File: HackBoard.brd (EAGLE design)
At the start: 68.6 x 61.6 mm, 45 parts, among them J1 USB MICRO, J2 8x1F-H8.5, J3 8x1F-H8.5, J4 6x1F-H8.5, P13 Yellow, U1 ATMEGA32U4-XUMU, U2 ATMEGA32U4-XUAU, U3 LP2985-33DBVR, Y1 16MHz KX-7

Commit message: Adición de 2 switch y 3 leds
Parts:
- added A: Amarillo, led:CHIPLED_0805
- added C10, C12: 100n, rcl:C0805
- added R: Rojo, led:CHIPLED_0805
- added R12, R13, R14, R15: 1K, resistor:M0805
- added SW1, SW2: (no value), switch-omron:B3F-10XX
- added V: Verde, led:CHIPLED_0805
- moved C11 0.51 mm to (30.2, 20.2)
- moved C4 0.51 mm to (48.8, 35.4)
- moved C5 0.51 mm to (57.1, 30.4)
- moved C7 0.51 mm to (57.1, 20.2)
- moved C8 0.51 mm to (6.99, 46.2)
- moved C9 0.51 mm to (58.4, 21.8)
- moved D2 0.51 mm to (58.9, 30.4)
- moved ICSP 0.51 mm to (64.9, 31.6)
- moved J1 0.51 mm to (1.45, 41.8)
- moved JP2 0.51 mm to (41.9, 59.2)
- moved L1 0.51 mm to (55.2, 30.4)
- moved L2 0.51 mm to (11.4, 36.7)
- moved ON 0.51 mm to (20.2, 40.8)
- moved R10 0.51 mm to (11.4, 43.3)
- moved R2 0.51 mm to (55.9, 18.0)
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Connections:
- new net LED_A: R14.2
- new net LED_R: R13.2
- new net LED_V: R15.2
- new net N$10: R15.1, V.A
- new net N$8: R.A, R13.1
- new net N$9: A.A, R14.1
- new net SW1: C10.2, SW1.1, SW1.2
- new net SW2: C12.2, R12.2, SW2.3, SW2.4
- net +5V: now also SW2.1, SW2.2
- net GND: now also A.C, C10.1, C12.1, R.C, R12.1, SW1.3, SW1.4, V.C
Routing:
- net +5V: track 258.3 -> 272.9 mm
- net SW2: track 0.00 -> 12.3 mm
- net SW1: track 0.00 -> 11.1 mm
- net N$9: track 0.00 -> 9.92 mm
- net N$8: track 0.00 -> 8.66 mm
- net N$10: track 0.00 -> 8.08 mm
- net GND: track 62.4 -> 63.5 mm, vias 18 -> 17
- net A4: track 24.3 -> 24.8 mm
- net VIN: track 3.56 -> 4.06 mm
- net N$6: track 3.56 -> 4.06 mm
- net A5: track 25.9 -> 26.4 mm
- net A3: track 22.7 -> 23.2 mm
- net A1: track 20.0 -> 20.5 mm
- net A0: track 18.7 -> 19.2 mm
- net A2: track 21.4 -> 21.9 mm
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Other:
- board size 68.6 x 61.6 mm -> 68.6 x 62.1 mm
- board text added: "HackBoard v0.2 hackbo.co"
- board text added: "Made In Colombia"

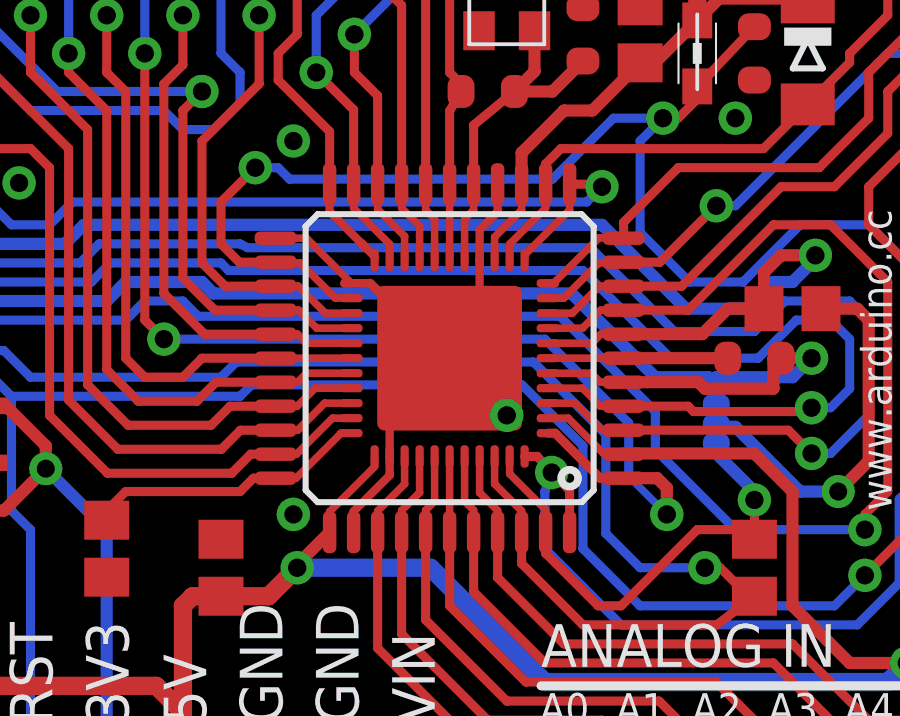
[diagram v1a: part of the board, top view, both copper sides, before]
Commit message: Se elimina Micro con encapsulado QFN
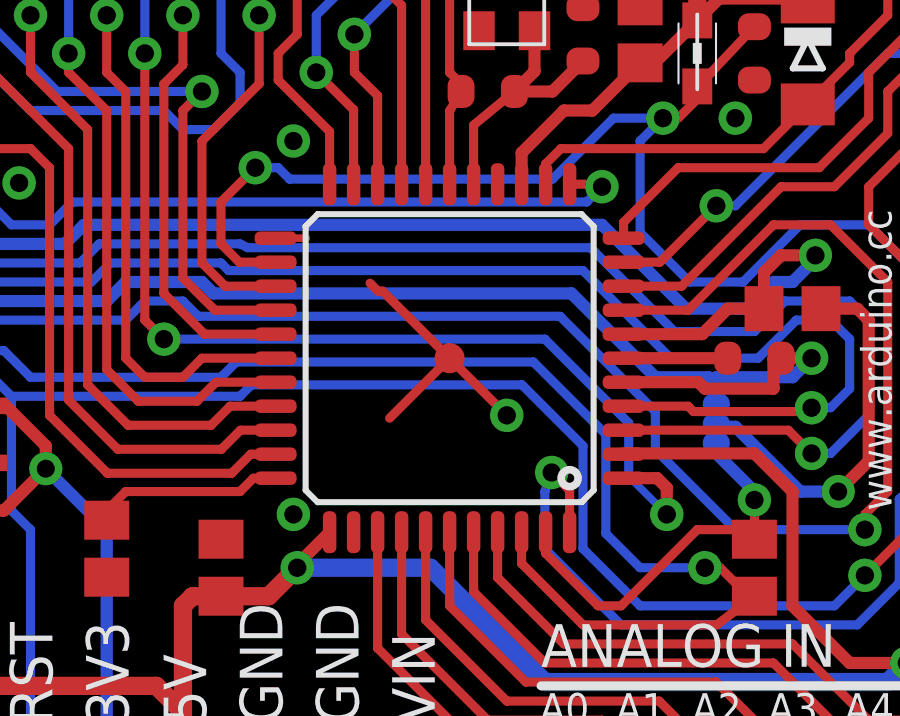
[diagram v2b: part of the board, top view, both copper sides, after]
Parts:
- removed U1: ATMEGA32U4-XUMU, SmartPrj:QFN44ML7X7
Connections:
- net +5V: no longer U1.14, U1.2, U1.34, U1.7
- net A0: no longer U1.36
- net A1: no longer U1.37
- net A2: no longer U1.38
- net A3: no longer U1.39
- net A4: no longer U1.40
- net A5: no longer U1.41
- net AGND: no longer U1.43
- net AREF: no longer U1.42
- net AVCC: no longer U1.24, U1.44
- net D0/RX: no longer U1.20
- net D1/TX: no longer U1.21
- net D2/SDA: no longer U1.19
- net D3/SCL: no longer U1.18
- net D4: no longer U1.25
- net D5*: no longer U1.31
- net D6*: no longer U1.27
- net D7: no longer U1.1
- net GND: no longer U1.15, U1.23, U1.35, U1.EXP
- net HWB: no longer U1.33
- net IO10*: no longer U1.30
- net IO11*: no longer U1.12
- net IO12: no longer U1.26
- net IO13*: no longer U1.32
- net IO8: no longer U1.28
- net IO9*: no longer U1.29
- net MISO: no longer U1.11
- net MOSI: no longer U1.10
- net RD+: no longer U1.4
- net RD-: no longer U1.3
- net RESET: no longer U1.13
- net RXLED: no longer U1.8
- net SCK: no longer U1.9
- net TXLED: no longer U1.22
- net UCAP: no longer U1.6
- net UGND: no longer U1.5
- net XTAL1: no longer U1.17
- net XTAL2: no longer U1.16
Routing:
- net GND: track 63.5 -> 50.0 mm
- net +5V: track 272.9 -> 261.2 mm
- net AVCC: track 73.5 -> 69.4 mm
- net TXLED: track 49.6 -> 46.3 mm
- net MISO: track 20.4 -> 17.2 mm
- net HWB: track 9.54 -> 6.40 mm
- net IO11*: track 62.6 -> 59.5 mm
- net D7: track 68.3 -> 65.1 mm
- net IO13*: track 64.7 -> 61.7 mm
- net D1/TX: track 46.2 -> 43.2 mm
- net AGND: track 16.8 -> 13.7 mm
- net RESET: track 165.9 -> 162.8 mm
- net MOSI: track 19.8 -> 16.8 mm
- net RD-: track 75.6 -> 72.7 mm
- net D5*: track 70.1 -> 67.2 mm
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
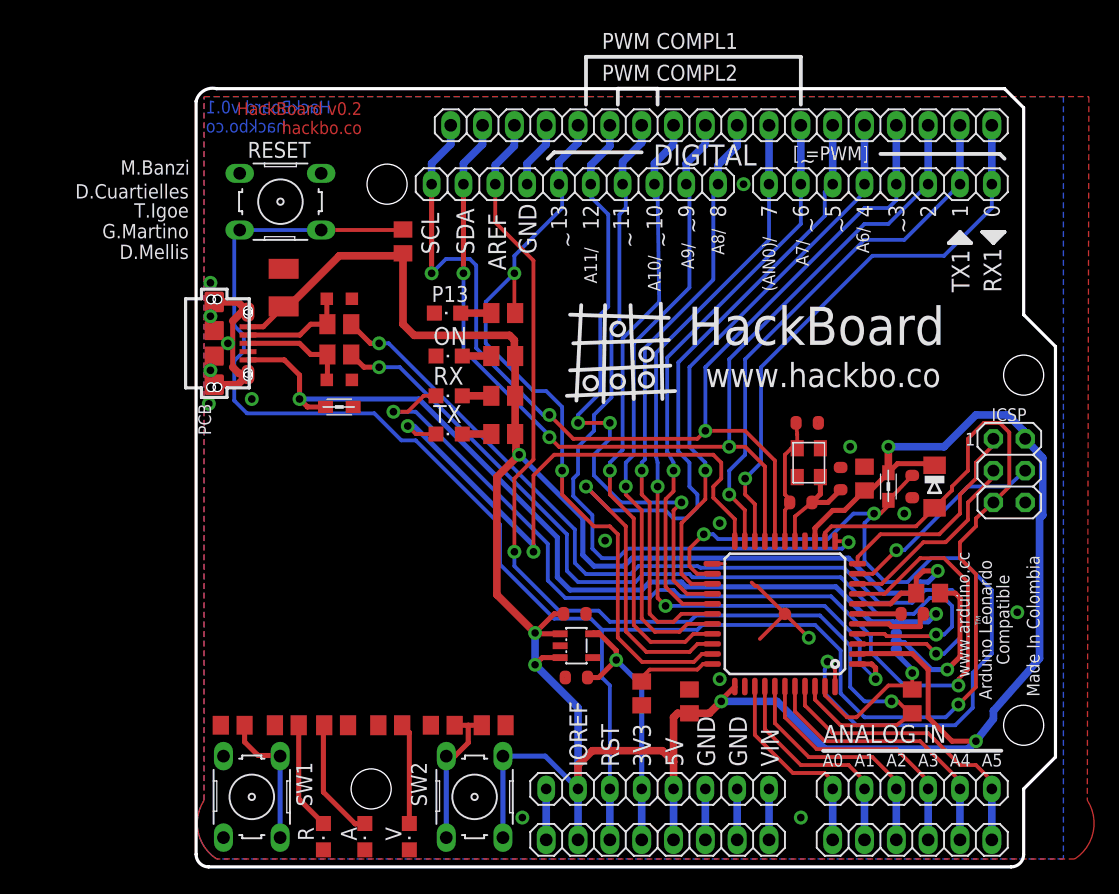
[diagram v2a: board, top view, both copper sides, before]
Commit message: Se modifica el nombre de la tarjeta a HackBoard 101
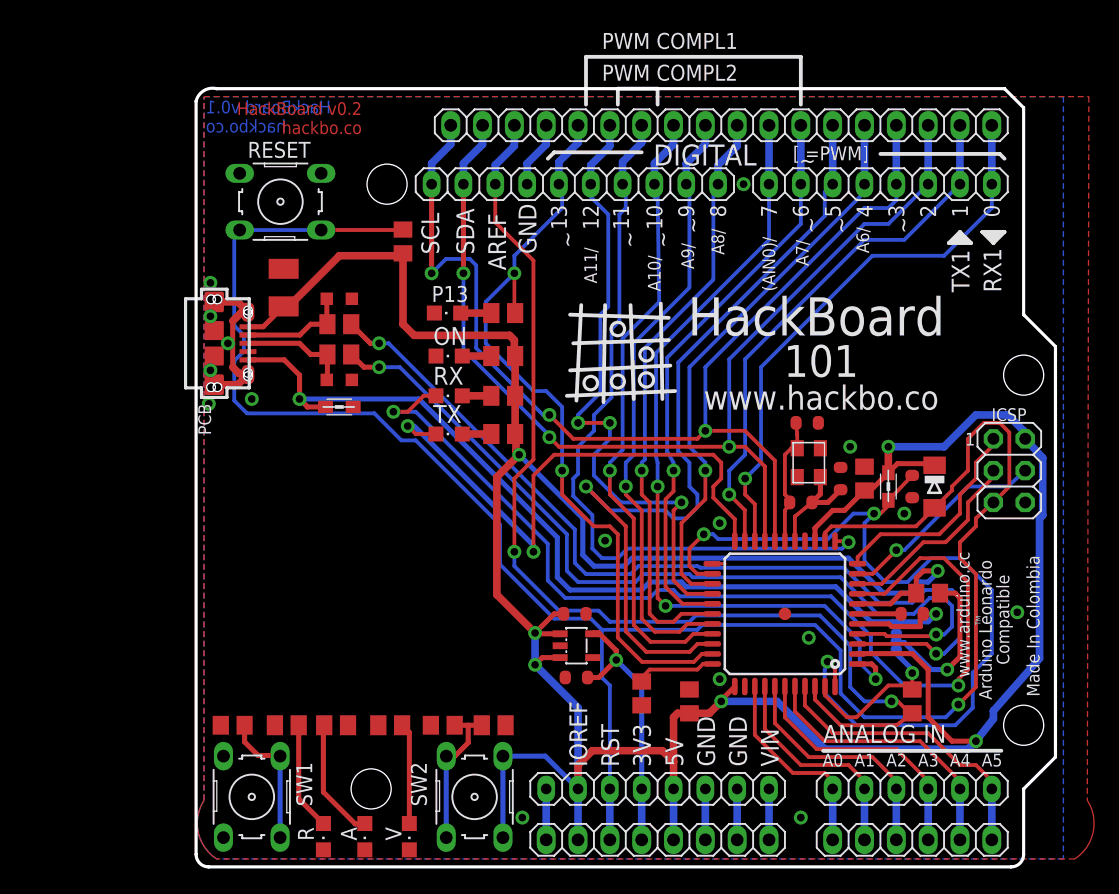
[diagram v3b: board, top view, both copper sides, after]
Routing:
- net GND: track 50.0 -> 40.7 mm
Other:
- board text added: "101"
- board text removed: "D.Cuartielles"
- board text removed: "D.Mellis"
- board text removed: "G.Martino"
- board text removed: "M.Banzi"
- board text removed: "T.Igoe"
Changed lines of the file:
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@@
 <layer number="21" name="tPlace" color="7" fill="1" visible="yes" active="yes"/>
 <layer number="22" name="bPlace" color="7" fill="1" visible="no" active="yes"/>
-<layer number="23" name="tOrigins" color="15" fill="1" visible="yes" active="yes"/>
+<layer number="23" name="tOrigins" color="15" fill="1" visible="no" active="yes"/>
 <layer number="24" name="bOrigins" color="15" fill="1" visible="no" active="yes"/>
 <layer number="25" name="tNames" color="7" fill="1" visible="yes" active="yes"/>
@@
 <text x="36.4854" y="55.9712" size="1.6764" layer="25" font="vector" ratio="15">DIGITAL</text>
 <text x="63.5" y="13.335" size="1.016" layer="25" font="vector" ratio="12" rot="R90">Arduino Leonardo</text>
-<text x="40.6618" y="38.289" size="1.9304" layer="25" font="vector" ratio="12">www.hackbo.co</text>
+<text x="40.5118" y="36.489" size="1.9304" layer="25" font="vector" ratio="12">www.hackbo.co</text>
 <text x="24.7352" y="47.6118" size="1.4224" layer="25" font="vector" ratio="10" rot="R90">AREF</text>
 <text x="61.3734" y="33.6274" size="1.016" layer="25" font="vector" ratio="15">1</text>
 <text x="27.159" y="48.9072" size="1.4224" layer="25" font="vector" ratio="10" rot="R90">GND</text>
-<text x="-0.508" y="56.388" size="1.143" layer="25" font="vector" ratio="12" rot="R180">M.Banzi</text>
-<text x="-0.5842" y="54.483" size="1.143" layer="25" font="vector" ratio="12" rot="R180">D.Cuartielles</text>
-<text x="-0.5842" y="49.657" size="1.143" layer="25" font="vector" ratio="12" rot="R180">D.Mellis</text>
 <text x="61.7176" y="45.8592" size="1.4224" layer="25" font="vector" ratio="10" rot="R90">TX1</text>
 <text x="64.262" y="45.847" size="1.4224" layer="25" font="vector" ratio="10" rot="R90">RX1</text>
 <text x="47.625" y="56.388" size="1.1176" layer="25" font="vector" ratio="13">[ =PWM]</text>
-<text x="-0.5842" y="51.308" size="1.143" layer="25" font="vector" ratio="12" rot="R180">G.Martino</text>
-<text x="-0.5842" y="52.959" size="1.143" layer="25" font="vector" ratio="12" rot="R180">T.Igoe</text>
 <text x="13.2298" y="61.022" size="1.016" layer="1" font="vector" ratio="12" rot="R180">HackBoard v0.2
 hackbo.co</text>
-<text x="39.243" y="41.656" size="3.048" layer="25" font="vector" ratio="15">HackBoard</text>
+<text x="39.243" y="42.406" size="3.048" layer="25" font="vector" ratio="15">HackBoard</text>
 <text x="33.7522" y="7.9878" size="1.4224" layer="25" font="vector" ratio="10" rot="R90">RST</text>
 <text x="36.2922" y="7.9878" size="1.4224" layer="25" font="vector" ratio="10" rot="R90">3V3</text>
@@
 <text x="61.722" y="15.113" size="1.016" layer="25" font="vector" ratio="12" rot="R90">www.arduino.cc</text>
 <text x="67.31" y="13.589" size="1.016" layer="25" font="vector" ratio="12" rot="R90">Made In Colombia</text>
+<text x="46.893" y="39.106" size="2.54" layer="25" font="vector" ratio="15">101</text>
 </plain>
 <attributes>
@@
 <wire x1="55.88" y1="17.9936" x2="55.88" y2="18.6586" width="0.4064" layer="16"/>
 <wire x1="42.215" y1="24.193" x2="41.19" y2="24.193" width="0.254" layer="1"/>
-<wire x1="44.99" y1="18.193" x2="46.99" y2="20.193" width="0.3048" layer="1"/>
-<wire x1="44.6024" y1="22.4282" x2="44.3376" y2="22.693" width="0.3048" layer="1"/>
-<wire x1="44.7548" y1="22.4282" x2="44.6024" y2="22.4282" width="0.3048" layer="1"/>
-<wire x1="46.99" y1="20.193" x2="44.7548" y2="22.4282" width="0.3048" layer="1"/>
-<wire x1="46.99" y1="20.193" x2="48.895" y2="18.288" width="0.3048" layer="1"/>
 <wire x1="3.3274" y1="45.085" x2="1.4478" y2="45.085" width="0.6096" layer="1"/>
 <wire x1="4.1402" y1="44.2722" x2="3.3274" y2="45.085" width="0.6096" layer="1"/>
